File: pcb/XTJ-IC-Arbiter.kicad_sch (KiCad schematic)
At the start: 34 parts, among them J3 DTM13-12PA-R008, SW1 SW_DIP_x01, SW2 SW_DIP_x01, U1 LM2672N-5.0, U3 Teensy4.0, U4 MCP2562-H-P, U5 SP723ABG

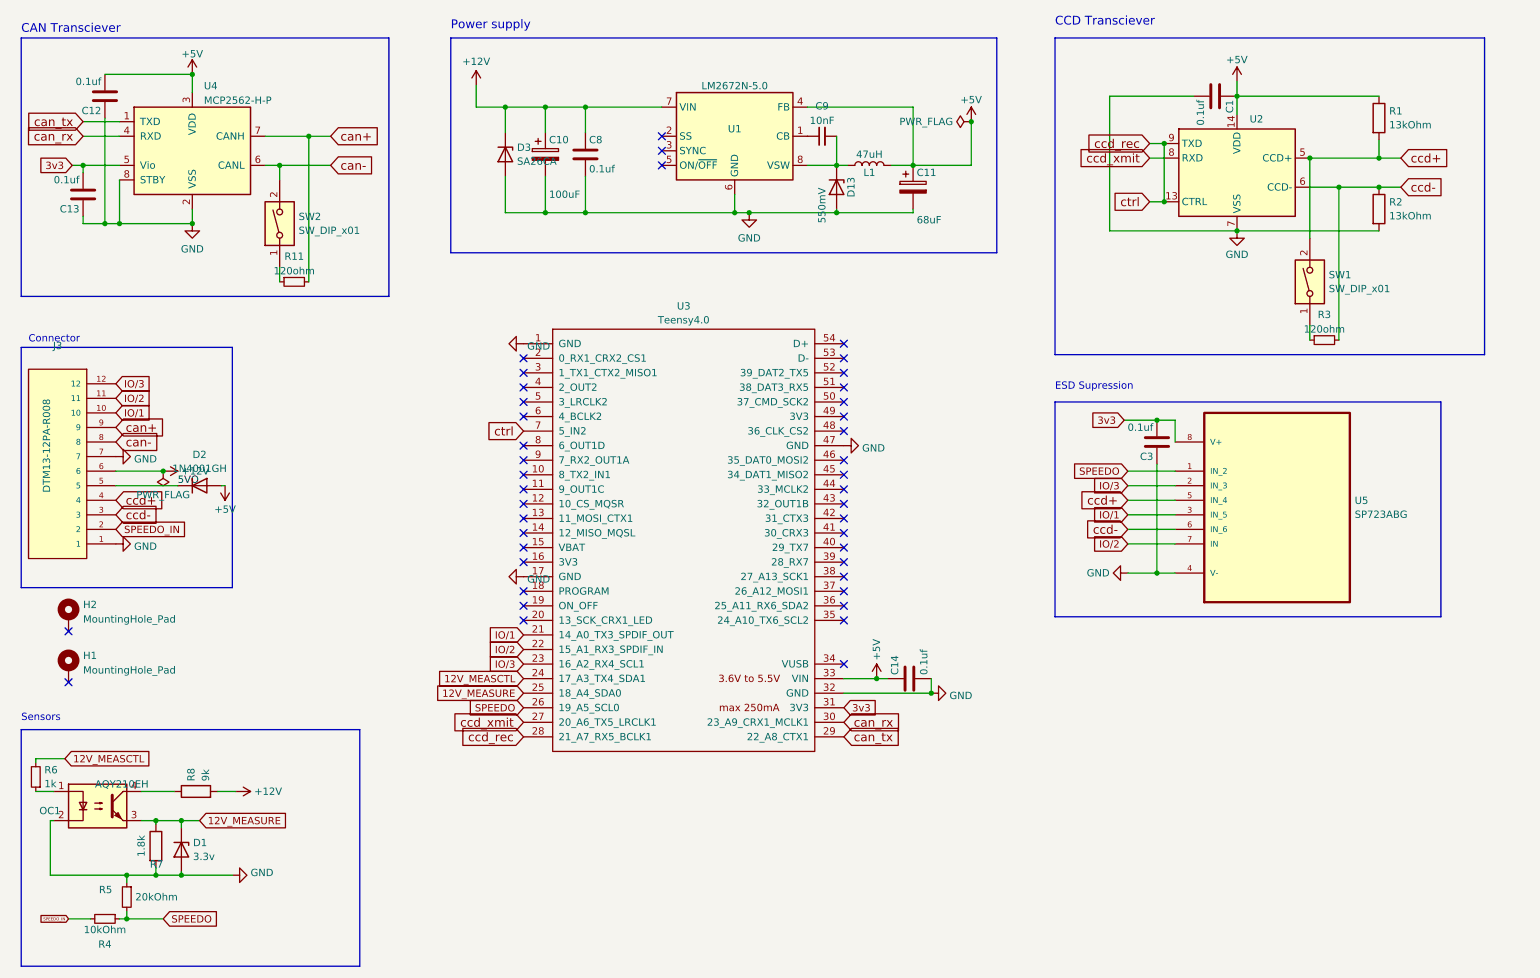
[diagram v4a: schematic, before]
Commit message: no battery relay
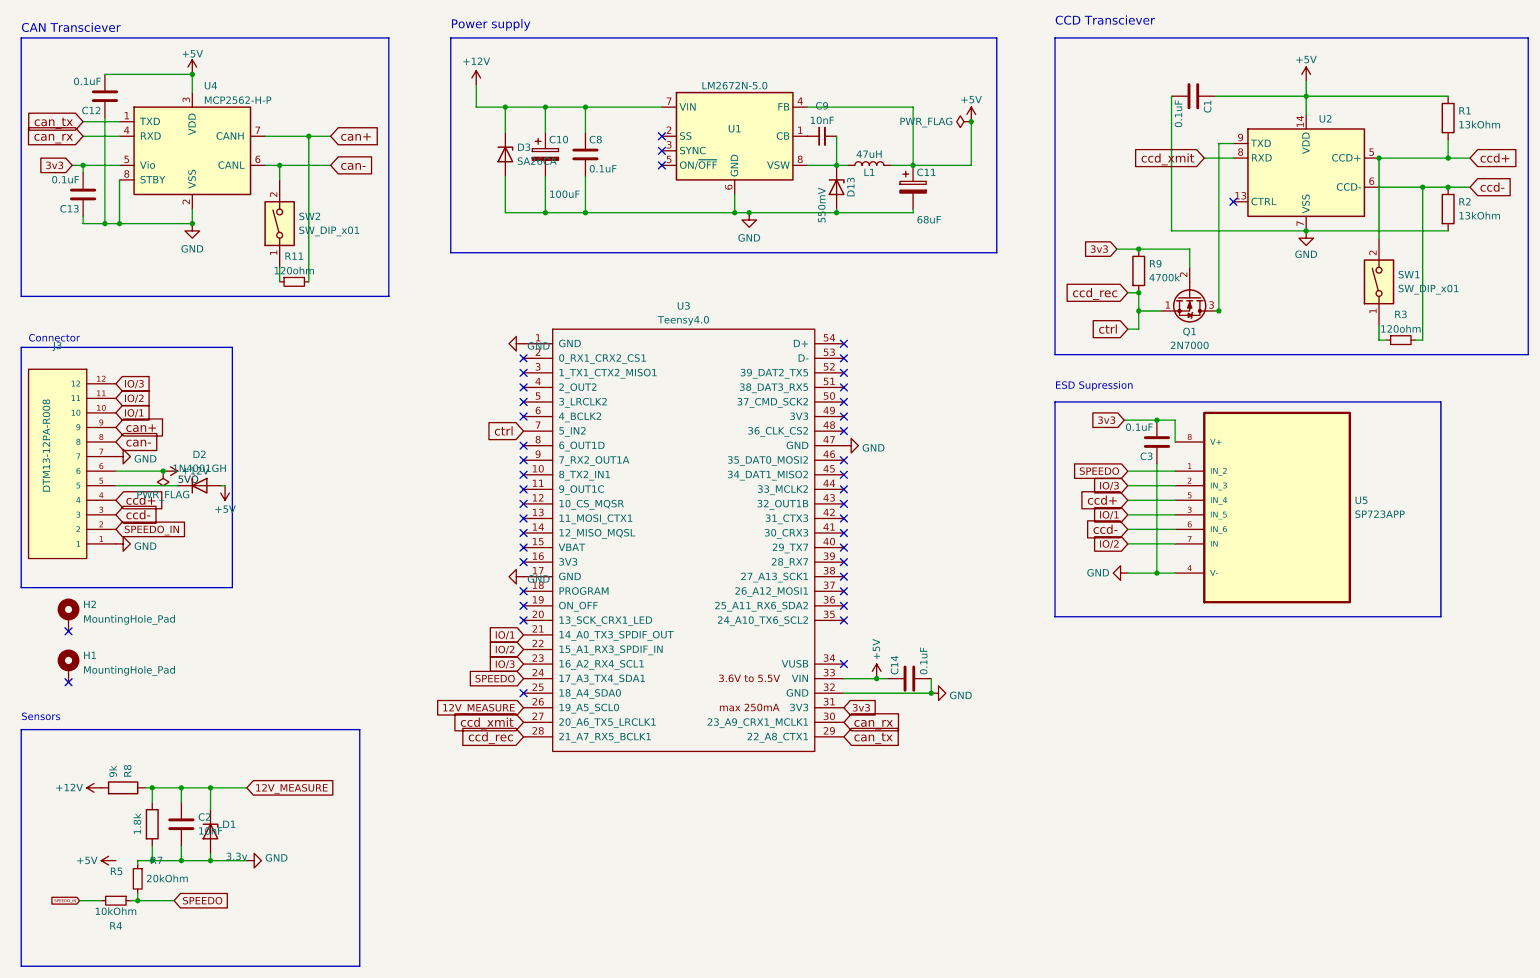
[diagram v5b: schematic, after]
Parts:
- removed OC1: AQY210EH, Package_DIP:DIP-4_W7.62mm, symbol Isolator:FODM217A
- removed R6: 1k, Resistor_THT:R_Axial_DIN0207_L6.3mm_D2.5mm_P7.62mm_Horizontal, symbol Device:R_Small
- added C2: 10nF, Capacitor_THT:C_Axial_L3.8mm_D2.6mm_P7.50mm_Horizontal, symbol Device:C
- added Q1: 2N7000, Package_TO_SOT_THT:TO-92_Inline, symbol Transistor_FET:2N7000
- added R9: 4700k, Resistor_THT:R_Axial_DIN0207_L6.3mm_D2.5mm_P7.62mm_Horizontal, symbol Device:R
- C1, C12, C13, C14, C3, C8: value 0.1uf -> 0.1uF
- U5: value SP723ABG -> SP723APP
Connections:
- net 12V_MEASCTL is gone; now on net SPEEDO: U3.24 (17_A3_TX4_SDA1)
- net 12V_MEASURE: now also R8.1, U3.26 (19_A5_SCL0), C2.1; no longer U3.25 (18_A4_SDA0)
- net 3v3: now also Q1.2 (G), R9.1
- net GND: now also C2.2
- net SPEEDO: no longer U3.26 (19_A5_SCL0)
- net ccd_rec: now also Q1.1 (S), R9.2; no longer U2.13 (CTRL), U2.9 (TXD)
- new net: Q1.3 (D), U2.9 (TXD)
- no-connect marks 42 -> 44
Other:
- moved on the sheet: C1, D1, R1, R2, R3, R4, R5, R7, R8, SW1, U2

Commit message: bigger courtyard for the ccd module
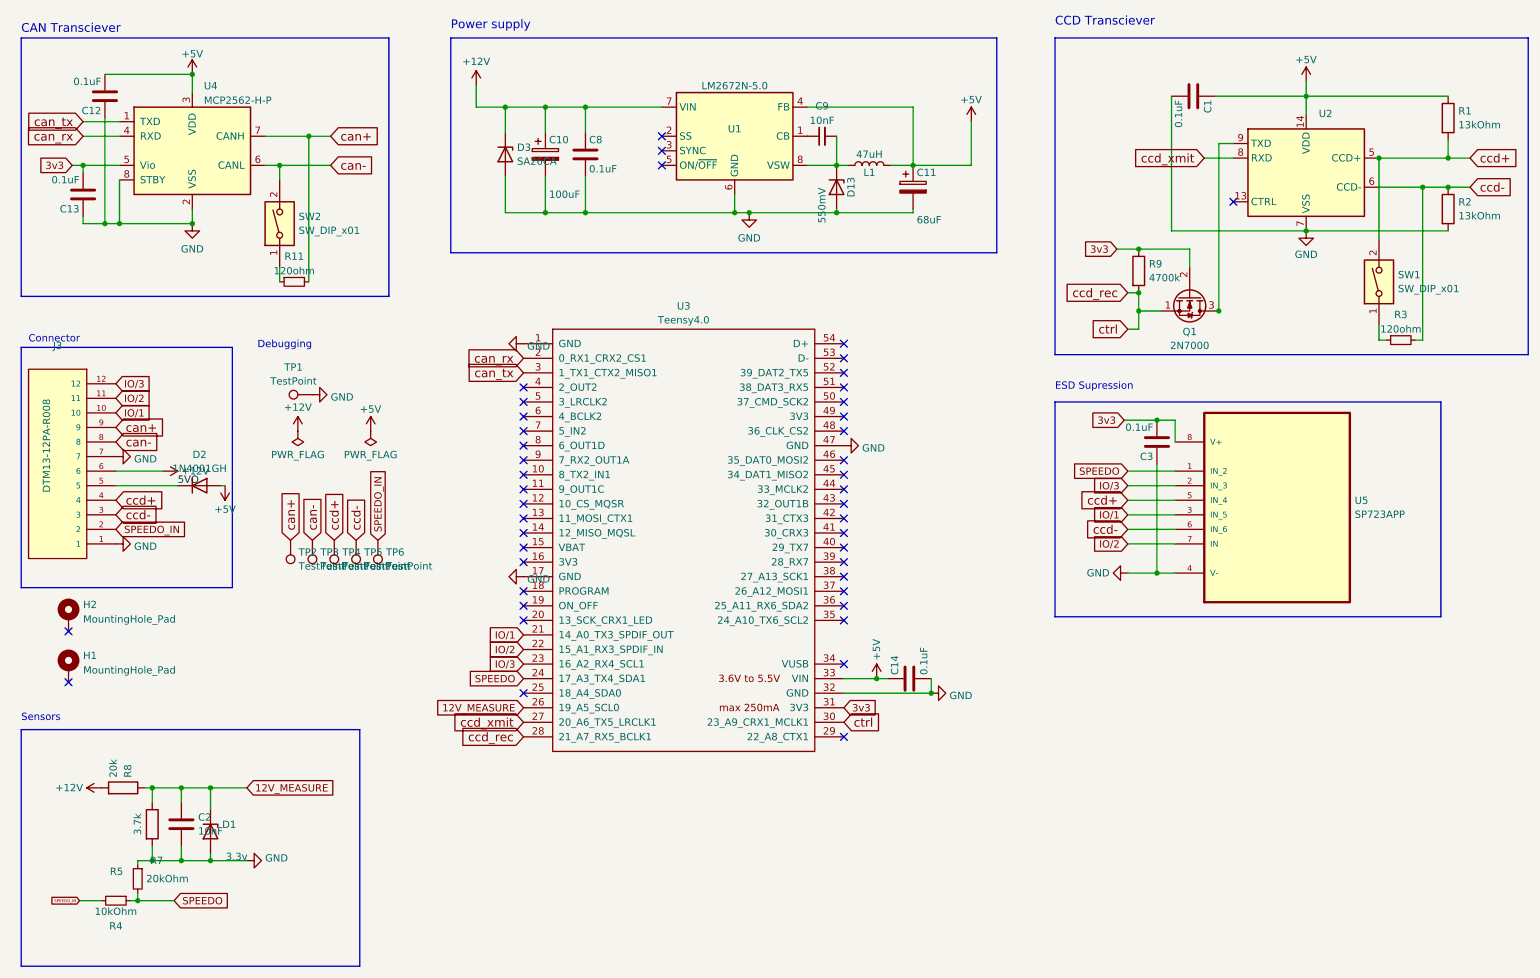
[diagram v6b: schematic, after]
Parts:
- added TP1, TP2, TP3, TP4, TP5, TP6: TestPoint, TestPoint:TestPoint_Loop_D2.50mm_Drill1.0mm, symbol Connector:TestPoint
- R7: value 1.8k -> 3.7k
- R8: value 9k -> 20k
- U2: footprint Package_DIP:DIP-14_W7.62mm -> parts:DIP-14_W7.62mm Bigger
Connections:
- net GND: now also TP1.1
- net SPEEDO_IN: now also TP6.1
- net can+: now also TP2.1
- net can-: now also TP3.1
- net can_rx: now also U3.2 (0_RX1_CRX2_CS1); no longer U3.30 (23_A9_CRX1_MCLK1)
- net can_tx: now also U3.3 (1_TX1_CTX2_MISO1); no longer U3.29 (22_A8_CTX1)
- net ccd+: now also TP4.1
- net ccd-: now also TP5.1
- net ccd_rec: now also U3.30 (23_A9_CRX1_MCLK1); no longer U3.7 (5_IN2)
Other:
- note added: "Debugging"

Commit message: tmp
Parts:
- removed TP2, TP3: TestPoint, TestPoint:TestPoint_Loop_D2.50mm_Drill1.0mm, symbol Connector:TestPoint
- added TP10, TP11, TP12, TP13, TP8, TP9: TestPoint, TestPoint:TestPoint_Loop_D2.50mm_Drill1.0mm, symbol Connector:TestPoint
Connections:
- net +5V: now also TP8.1
- net 3v3: now also TP9.1
- net SPEEDO: no longer U5.1 (IN_2)
- net SPEEDO_IN: now also U5.1 (IN_2)
- net can_rx: now also TP10.1
- net can_tx: now also TP11.1
- net ccd_rec: now also TP13.1
- net ccd_xmit: now also TP12.1
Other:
- moved on the sheet: C3, U5

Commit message: Update to KiCad 9
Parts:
- D2: value 1N4001GH -> 1N4001GH
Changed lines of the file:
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@@
 (kicad_sch
-	(version 20231120)
+	(version 20250114)
 	(generator "eeschema")
-	(generator_version "8.0")
+	(generator_version "9.0")
 	(paper "A4")
 	(title_block
@@
 		(company "N9 Works")
 	)
+	(rectangle
+		(start 198.12 87.63)
+		(end 265.43 125.095)
+		(stroke
+			(width 0)
+			(type default)
+		)
+		(fill
+			(type none)
+		)
+	)
+	(rectangle
+		(start 17.78 144.78)
+		(end 76.835 186.055)
+		(stroke
+			(width 0)
+			(type default)
+		)
+		(fill
+			(type none)
+		)
+	)
+	(rectangle
+		(start 17.78 78.105)
+		(end 54.61 120.015)
+		(stroke
+			(width 0)
+			(type default)
+		)
+		(fill
+			(type none)
+		)
+	)
+	(text "CAN Transciever"
+		(exclude_from_sim no)
+		(at 17.78 23.495 0)
+		(effects
+			(font
+				(size 1.524 1.524)
+			)
+			(justify left bottom)
+		)
+	)
+	(text "Debugging"
+		(exclude_from_sim no)
+		(at 63.754 77.724 0)
+		(effects
+			(font
+				(size 1.27 1.27)
+			)
+		)
+	)
+	(text "Sensors"
+		(exclude_from_sim no)
+		(at 17.78 143.51 0)
+		(effects
+			(font
+				(size 1.27 1.27)
+			)
+			(justify left bottom)
+		)
+	)
+	(text "CCD Transciever"
+		(exclude_from_sim no)
+		(at 198.12 22.225 0)
+		(effects
+			(font
+				(size 1.524 1.524)
+			)
+			(justify left bottom)
+		)
+	)
+	(text "ESD Supression"
+		(exclude_from_sim no)
+		(at 198.12 85.725 0)
+		(effects
+			(font
+				(size 1.27 1.27)
+			)
+			(justify left bottom)
+		)
+	)
+	(text "Power supply"
+		(exclude_from_sim no)
+		(at 92.71 22.86 0)
+		(effects
+			(font
+				(size 1.524 1.524)
+			)
+			(justify left bottom)
+		)
+	)
+	(text "Connector"
+		(exclude_from_sim no)
+		(at 19.05 77.47 0)
+		(effects
+			(font
+				(size 1.27 1.27)
+			)
+			(justify left bottom)
+		)
+	)
 	(junction
 		(at 266.7 50.165)
@@
 		)
 	)
-	(rectangle
-		(start 198.12 87.63)
-		(end 265.43 125.095)
-		(stroke
-			(width 0)
-			(type default)
-		)
-		(fill
-			(type none)
-		)
-	)
-	(rectangle
-		(start 17.78 144.78)
-		(end 76.835 186.055)
-		(stroke
-			(width 0)
-			(type default)
-		)
-		(fill
-			(type none)
-		)
-	)
-	(rectangle
-		(start 17.78 78.105)
-		(end 54.61 120.015)
-		(stroke
-			(width 0)
-			(type default)
-		)
-		(fill
-			(type none)
-		)
-	)
-	(text "CAN Transciever"
-		(exclude_from_sim no)
-		(at 17.78 23.495 0)
-		(effects
-			(font
-				(size 1.524 1.524)
-			)
-			(justify left bottom)
-		)
-	)
-	(text "Debugging"
-		(exclude_from_sim no)
-		(at 63.754 77.724 0)
-		(effects
-			(font
-				(size 1.27 1.27)
-			)
-		)
-	)
-	(text "Sensors"
-		(exclude_from_sim no)
-		(at 17.78 143.51 0)
-		(effects
-			(font
-				(size 1.27 1.27)
-			)
-			(justify left bottom)
-		)
-	)
-	(text "CCD Transciever"
-		(exclude_from_sim no)
-		(at 198.12 22.225 0)
-		(effects
-			(font
-				(size 1.524 1.524)
-			)
-			(justify left bottom)
-		)
-	)
-	(text "ESD Supression"
-		(exclude_from_sim no)
-		(at 198.12 85.725 0)
-		(effects
-			(font
-				(size 1.27 1.27)
-			)
-			(justify left bottom)
-		)
-	)
-	(text "Power supply"
-		(exclude_from_sim no)
-		(at 92.71 22.86 0)
-		(effects
-			(font
-				(size 1.524 1.524)
-			)
-			(justify left bottom)
-		)
-	)
-	(text "Connector"
-		(exclude_from_sim no)
-		(at 19.05 77.47 0)
-		(effects
-			(font
-				(size 1.27 1.27)
-			)
-			(justify left bottom)
-		)
-	)
 	(label "5VO"
 		(at 45.085 102.235 0)
-		(fields_autoplaced yes)
 		(effects
 			(font
@@
 			)
 		)
-		(property "Value" "1N4001GH "
+		(property "Value" "1N4001GH"
 			(at 48.895 99.2449 0)
 			(effects
@@
 		)
 	)
+	(embedded_fonts no)
 )
